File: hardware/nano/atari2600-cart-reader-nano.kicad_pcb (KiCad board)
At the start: 2 copper layers, 80 x 62 mm, 16 parts, among them J1 Atari 2600 Cartridge-Slot, Q1 BC327, U1 MCP23017-E/SP

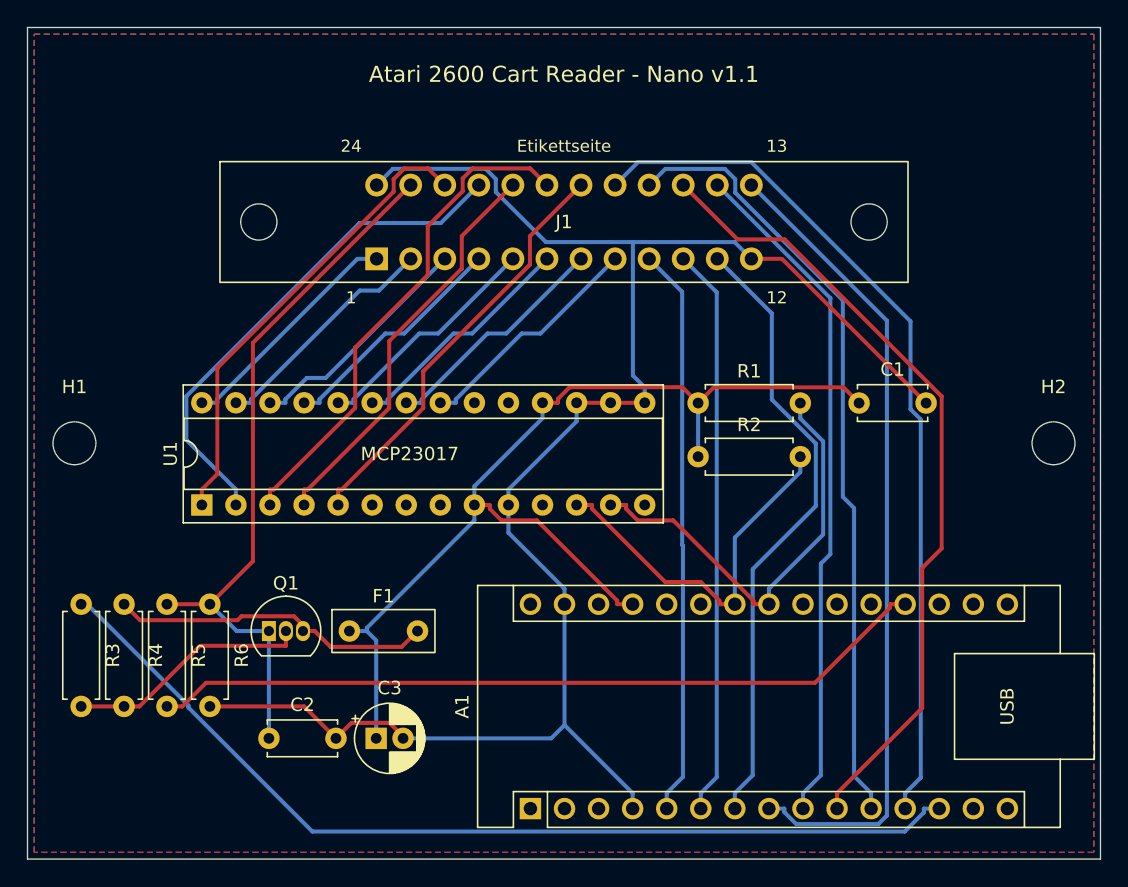
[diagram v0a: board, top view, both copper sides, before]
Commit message: Silkscreen: reference and value per part, fambach.net on the front
labels.py adds the silkscreen texts after routing, so the copper stays unchanged.

Co-Authored-By: Claude Opus 5.5 <noreply@anthropic.com>
Claude-Session: https://claude.ai/code/session_015VQCpzuZ22TPQEmx9cLrbH
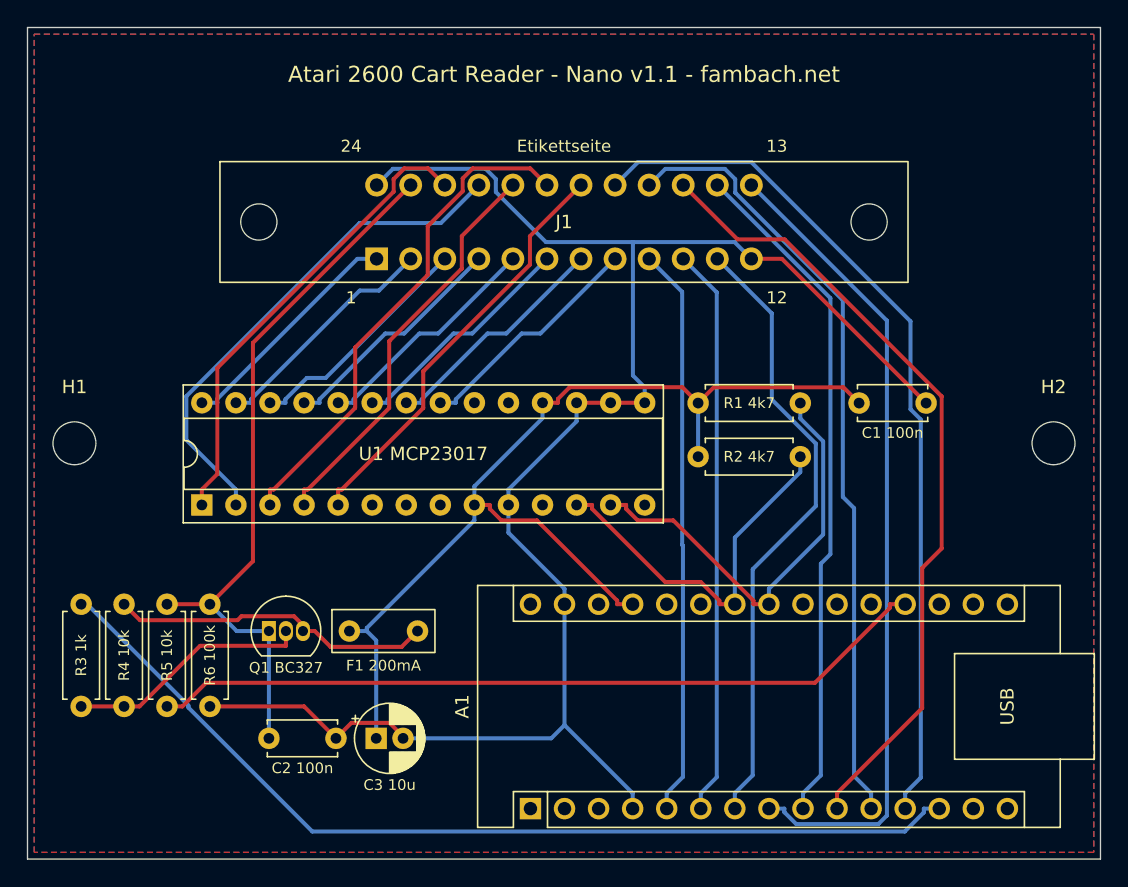
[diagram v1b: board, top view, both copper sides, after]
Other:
- board text added: "Atari 2600 Cart Reader - Nano v1.1 - fambach.net"
- board text added: "C1 100n"
- board text added: "C2 100n"
- board text added: "C3 10u"
- board text added: "F1 200mA"
- board text added: "Q1 BC327"
- board text added: "R1 4k7"
- board text added: "R2 4k7"
- board text added: "R3 1k"
- board text added: "R4 10k"
- board text added: "R5 10k"
- board text added: "R6 100k"
- board text added: "U1 MCP23017"
- board text removed: "Atari 2600 Cart Reader - Nano v1.1"
- board text removed: "MCP23017"
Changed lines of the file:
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@@
     (tags "Resistor Axial_DIN0207 series Axial Horizontal pin pitch 7.62mm 0.25W = 1/4W length 6.3mm diameter 2.5mm")
     (attr through_hole)
-    (fp_text reference "R6" (at 3.81 -2.37 -90) (layer "F.SilkS")
+    (fp_text reference "R6" (at 3.81 -2.37 -90) (layer "F.SilkS") hide
         (effects (font (size 1 1) (thickness 0.15)))
     )
@@
     (tags "Resistor Axial_DIN0207 series Axial Horizontal pin pitch 7.62mm 0.25W = 1/4W length 6.3mm diameter 2.5mm")
     (attr through_hole)
-    (fp_text reference "R1" (at 3.81 -2.37) (layer "F.SilkS")
+    (fp_text reference "R1" (at 3.81 -2.37) (layer "F.SilkS") hide
         (effects (font (size 1 1) (thickness 0.15)))
     )
@@
     (tags "CP Radial series Radial pin pitch 2.00mm  diameter 5mm Electrolytic Capacitor")
     (attr through_hole)
-    (fp_text reference "C3" (at 1 -3.75) (layer "F.SilkS")
+    (fp_text reference "C3" (at 1 -3.75) (layer "F.SilkS") hide
         (effects (font (size 1 1) (thickness 0.15)))
     )
@@
     (tags "Resistor Axial_DIN0207 series Axial Horizontal pin pitch 7.62mm 0.25W = 1/4W length 6.3mm diameter 2.5mm")
     (attr through_hole)
-    (fp_text reference "R4" (at 3.81 -2.37 -90) (layer "F.SilkS")
+    (fp_text reference "R4" (at 3.81 -2.37 -90) (layer "F.SilkS") hide
         (effects (font (size 1 1) (thickness 0.15)))
     )
@@
     (tags "to-92 sc-43 sc-43a sot54 PA33 transistor")
     (attr through_hole)
-    (fp_text reference "Q1" (at 1.27 -3.56) (layer "F.SilkS")
+    (fp_text reference "Q1" (at 1.27 -3.56) (layer "F.SilkS") hide
         (effects (font (size 1 1) (thickness 0.15)))
     )
@@
     (tags "Resistor Axial_DIN0207 series Axial Horizontal pin pitch 7.62mm 0.25W = 1/4W length 6.3mm diameter 2.5mm")
     (attr through_hole)
-    (fp_text reference "R2" (at 3.81 -2.37) (layer "F.SilkS")
+    (fp_text reference "R2" (at 3.81 -2.37) (layer "F.SilkS") hide
         (effects (font (size 1 1) (thickness 0.15)))
     )
@@
     (tags "polyfuse PTC radial")
     (attr through_hole)
-    (fp_text reference "F1" (at 2.54 -2.6) (layer "F.SilkS")
+    (fp_text reference "F1" (at 2.54 -2.6) (layer "F.SilkS") hide
         (effects (font (size 1 1) (thickness 0.15)))
     )
@@
     (tags "THT DIP DIL PDIP 2.54mm 7.62mm 300mil Socket")
     (attr through_hole)
-    (fp_text reference "U1" (at 3.81 -2.33 90) (layer "F.SilkS")
+    (fp_text reference "U1" (at 3.81 -2.33 90) (layer "F.SilkS") hide
         (effects (font (size 1 1) (thickness 0.15)))
     )
@@
     (tags "C Disc series Radial pin pitch 5.00mm  diameter 5mm width 2.5mm Capacitor")
     (attr through_hole)
-    (fp_text reference "C2" (at 2.5 -2.5) (layer "F.SilkS")
+    (fp_text reference "C2" (at 2.5 -2.5) (layer "F.SilkS") hide
         (effects (font (size 1 1) (thickness 0.15)))
     )
@@
     (tags "Resistor Axial_DIN0207 series Axial Horizontal pin pitch 7.62mm 0.25W = 1/4W length 6.3mm diameter 2.5mm")
     (attr through_hole)
-    (fp_text reference "R5" (at 3.81 -2.37 -90) (layer "F.SilkS")
+    (fp_text reference "R5" (at 3.81 -2.37 -90) (layer "F.SilkS") hide
         (effects (font (size 1 1) (thickness 0.15)))
     )
@@
     (tags "Resistor Axial_DIN0207 series Axial Horizontal pin pitch 7.62mm 0.25W = 1/4W length 6.3mm diameter 2.5mm")
     (attr through_hole)
-    (fp_text reference "R3" (at 3.81 -2.37 -90) (layer "F.SilkS")
+    (fp_text reference "R3" (at 3.81 -2.37 -90) (layer "F.SilkS") hide
         (effects (font (size 1 1) (thickness 0.15)))
     )
@@
     (tags "C Disc series Radial pin pitch 5.00mm  diameter 5mm width 2.5mm Capacitor")
     (attr through_hole)
-    (fp_text reference "C1" (at 2.5 -2.5) (layer "F.SilkS")
+    (fp_text reference "C1" (at 2.5 -2.5) (layer "F.SilkS") hide
         (effects (font (size 1 1) (thickness 0.15)))
     )
@@
   (gr_line (start 100 100) (end 180 100)
     (stroke (width 0.1) (type default)) (layer "Edge.Cuts"))
+  (gr_text "fambach.net" (at 140 137.5) (layer "B.SilkS")
+    (effects (font (size 1 1) (thickness 0.15)) (justify mirror))
+  )
   (gr_text "github.com/sfambach/arduino-atari2600-cart-reader" (at 140 139.5) (layer "B.SilkS")
     (effects (font (size 0.8 0.8) (thickness 0.12)) (justify mirror))
   )
-  (gr_text "fambach.net" (at 140 137.5) (layer "B.SilkS")
-    (effects (font (size 1 1) (thickness 0.15)) (justify mirror))
-  )
-  (gr_text "MCP23017" (at 128.5 131.8) (layer "F.SilkS")
+  (gr_text "R1 4k7" (at 153.81 128) (layer "F.SilkS")
+    (effects (font (size 0.8 0.8) (thickness 0.12)))
+  )
+  (gr_text "Atari 2600 Cart Reader - Nano v1.1 - fambach.net" (at 140 103.5) (layer "F.SilkS")
+    (effects (font (size 1.2 1.2) (thickness 0.18)))
+  )
+  (gr_text "F1 200mA" (at 126.54 147.575) (layer "F.SilkS")
+    (effects (font (size 0.8 0.8) (thickness 0.12)))
+  )
+  (gr_text "R5 10k" (at 110.4 146.81 90) (layer "F.SilkS")
+    (effects (font (size 0.8 0.8) (thickness 0.12)))
+  )
+  (gr_text "U1 MCP23017" (at 129.51 131.789999) (layer "F.SilkS")
     (effects (font (size 1 1) (thickness 0.15)))
   )
-  (gr_text "Atari 2600 Cart Reader - Nano v1.1" (at 140 103.5) (layer "F.SilkS")
-    (effects (font (size 1.2 1.2) (thickness 0.18)))
+  (gr_text "R4 10k" (at 107.2 146.81 90) (layer "F.SilkS")
+    (effects (font (size 0.8 0.8) (thickness 0.12)))
+  )
+  (gr_text "R6 100k" (at 113.599999 146.81 90) (layer "F.SilkS")
+    (effects (font (size 0.8 0.8) (thickness 0.12)))
+  )
+  (gr_text "C3 10u" (at 127 156.475) (layer "F.SilkS")
+    (effects (font (size 0.8 0.8) (thickness 0.12)))
+  )
+  (gr_text "Q1 BC327" (at 119.27 147.735) (layer "F.SilkS")
+    (effects (font (size 0.8 0.8) (thickness 0.12)))
+  )
+  (gr_text "R3 1k" (at 104 146.81 90) (layer "F.SilkS")
+    (effects (font (size 0.8 0.8) (thickness 0.12)))
+  )
+  (gr_text "R2 4k7" (at 153.81 132) (layer "F.SilkS")
+    (effects (font (size 0.8 0.8) (thickness 0.12)))
+  )
+  (gr_text "C1 100n" (at 164.5 130.225) (layer "F.SilkS")
+    (effects (font (size 0.8 0.8) (thickness 0.12)))
+  )
+  (gr_text "C2 100n" (at 120.5 155.225) (layer "F.SilkS")
+    (effects (font (size 0.8 0.8) (thickness 0.12)))
   )
   (segment (start 167 128) (end 156.25 117.25) (width 0.3) (layer "F.Cu") (net 1))

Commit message: Reset and read buttons on all boards (v1.2)
SW1 resets the Arduino, SW2 on A1 repeats the last dump; dump.py listen saves button dumps.

Co-Authored-By: Claude Opus 5.5 <noreply@anthropic.com>
Claude-Session: https://claude.ai/code/session_015VQCpzuZ22TPQEmx9cLrbH
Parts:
- added SW1: Reset, Button_Switch_THT:SW_PUSH_6mm, F.Cu at (161.0, 134.0)
- added SW2: Read, Button_Switch_THT:SW_PUSH_6mm, F.Cu at (103.0, 153.5)
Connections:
- A1 pad 20: (no net) -> /READ
- A1 pad 3: (no net) -> /RESET
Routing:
- net /READ: track 0.00 -> 64.9 mm
- net /RESET: track 0.00 -> 47.8 mm
- net GND: track 131.8 -> 166.9 mm
- net /D1: track 42.5 -> 52.1 mm, vias 0 -> 1
- net /D3: track 60.9 -> 53.7 mm
- net /A10: track 37.6 -> 44.3 mm
- net /SDA: track 32.6 -> 28.5 mm
- net /D0: track 42.5 -> 44.9 mm
- net /D6: track 58.4 -> 59.8 mm
- net /CART_SENSE: track 58.4 -> 59.8 mm
- net /D4: track 50.8 -> 52.1 mm
- net /D5: track 59.8 -> 60.6 mm
- net /A9: track 38.0 -> 38.8 mm
- net /CART_PWR: track 72.0 -> 72.7 mm
- net +5V: track 76.9 -> 76.2 mm
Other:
- board text added: "Atari 2600 Cart Reader - Nano v1.2 - fambach.net"
- board text added: "SW1 Reset"
- board text added: "SW2 Read"
- board text removed: "Atari 2600 Cart Reader - Nano v1.1 - fambach.net"

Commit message: Nano board: read button only, the Nano's own reset button stays reachable
Co-Authored-By: Claude Opus 5.5 <noreply@anthropic.com>
Claude-Session: https://claude.ai/code/session_015VQCpzuZ22TPQEmx9cLrbH
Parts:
- removed SW1: Reset, Button_Switch_THT:SW_PUSH_6mm
- moved SW2 61.2 mm to (161.0, 134.0)
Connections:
- A1 pad 3: /RESET -> (no net)
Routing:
- net /READ: track 64.9 -> 16.3 mm
- net /RESET: track 47.8 -> 0.00 mm
- net GND: track 166.9 -> 151.3 mm
- net /D3: track 53.7 -> 67.1 mm
- net /A10: track 44.3 -> 33.3 mm
- net /D1: track 52.1 -> 41.6 mm, vias 1 -> 0
- net /D5: track 60.6 -> 51.2 mm
- net /D4: track 52.1 -> 58.9 mm
- net /SCL: track 28.2 -> 32.2 mm
- net /D0: track 44.9 -> 42.1 mm
- net /D6: track 59.8 -> 57.2 mm
- net +5V: track 76.2 -> 78.6 mm
- net /D7: track 64.3 -> 62.4 mm
- net /D2: track 47.0 -> 48.2 mm
- net /A9: track 38.8 -> 37.8 mm
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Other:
- board text removed: "SW1 Reset"

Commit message: Uno/Nano: address bus via two 74HC595 on SPI, MCP23017 boards kept as variants
hal.h selects the MCP23017 with #define ADDR_MCP23017.

Co-Authored-By: Claude Opus 5.5 <noreply@anthropic.com>
Claude-Session: https://claude.ai/code/session_015VQCpzuZ22TPQEmx9cLrbH
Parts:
- removed R1, R2: 4k7, Resistor_THT:R_Axial_DIN0207_L6.3mm_D2.5mm_P7.62mm_Horizontal
- added C4: 100n, Capacitor_THT:C_Disc_D5.0mm_W2.5mm_P5.00mm, F.Cu at (162.0, 131.0)
- added U2: 74HC595, Package_DIP:DIP-16_W7.62mm_Socket, F.Cu at (134.9, 135.6)
- U1: value MCP23017-E/SP -> 74HC595; footprint Package_DIP:DIP-28_W7.62mm_Socket -> Package_DIP:DIP-16_W7.62mm_Socket
- moved C1 2.50 mm to (162.0, 125.5)
- moved SW2 0.20 mm to (161.0, 134.2)
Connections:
- A1 pad 14: (no net) -> /MOSI
- A1 pad 16: (no net) -> /SCK
- A1 pad 21: (no net) -> /LATCH
- A1 pad 23: /SDA -> (no net)
- A1 pad 24: /SCL -> (no net)
- U1 pad 1: /A8 -> /A1
- U1 pad 10: GND -> +5V
- U1 pad 11: (no net) -> /SCK
- U1 pad 12: /SCL -> /LATCH
- U1 pad 13: /SDA -> GND
- U1 pad 14: (no net) -> /MOSI
- U1 pad 15: GND -> /A0
- U1 pad 16: GND -> +5V
- U1 pad 2: /A9 -> /A2
- U1 pad 3: /A10 -> /A3
- U1 pad 4: /A11 -> /A4
- U1 pad 5: /A12 -> /A5
- U1 pad 6: (no net) -> /A6
- U1 pad 7: (no net) -> /A7
- U1 pad 8: (no net) -> GND
- U1 pad 9: +5V -> /SR_CHAIN
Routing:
- net /MOSI: track 0.00 -> 66.4 mm
- net /SCK: track 0.00 -> 58.9 mm, vias 0 -> 1
- net /LATCH: track 0.00 -> 47.5 mm
- net +5V: track 78.6 -> 119.4 mm
- net /SCL: track 32.2 -> 0.00 mm
- net /A6: track 17.6 -> 46.3 mm
- net /SDA: track 28.3 -> 0.00 mm
- net /A2: track 17.6 -> 44.9 mm
- net /A3: track 17.6 -> 42.9 mm, vias 1 -> 0
- net GND: track 151.3 -> 175.4 mm
- net /A1: track 17.6 -> 39.8 mm
- net /A8: track 34.4 -> 18.9 mm
- net /A0: track 17.6 -> 32.9 mm
- net /A9: track 37.8 -> 27.4 mm
- net /SR_CHAIN: track 0.00 -> 10.3 mm
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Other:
- board text added: "C4 100n"
- board text added: "U1 74HC595"
- board text added: "U2 74HC595"
- board text removed: "R1 4k7"
- board text removed: "R2 4k7"
- board text removed: "U1 MCP23017"
